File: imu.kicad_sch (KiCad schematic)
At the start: 21 parts, among them J1 Conn_01x06, U1 LSM6DSL, U2 LIS2MDL, U3 AMS1117-3.3

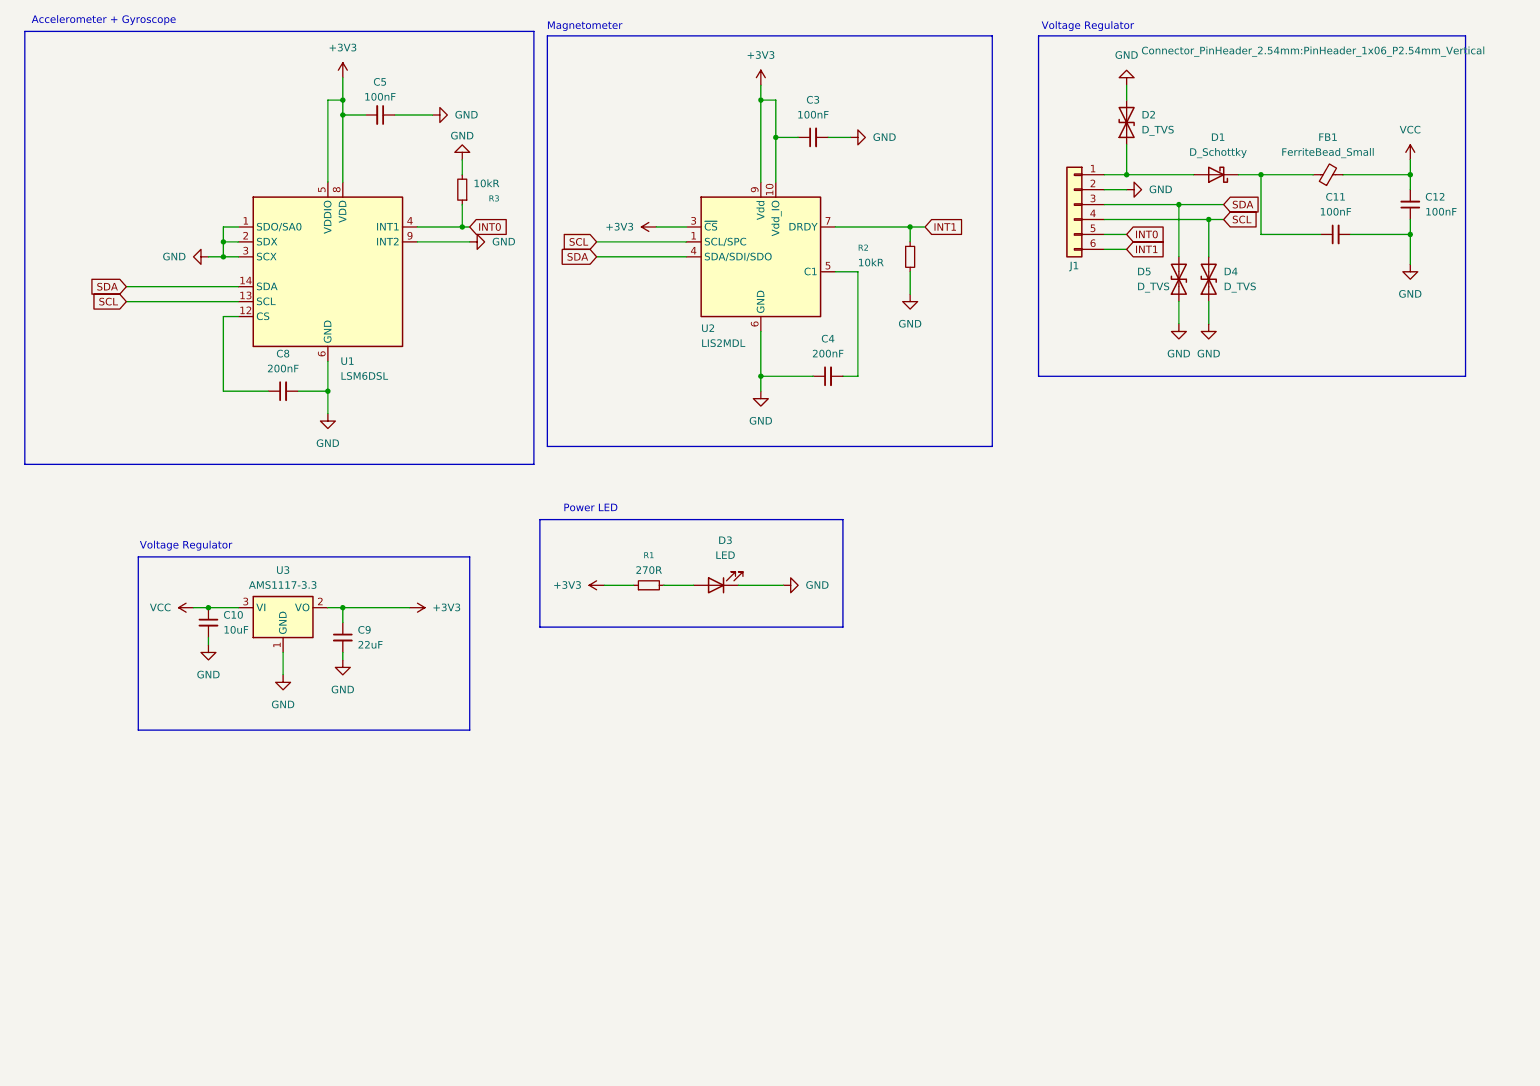
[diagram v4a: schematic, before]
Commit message: Add Fabrication Outputs
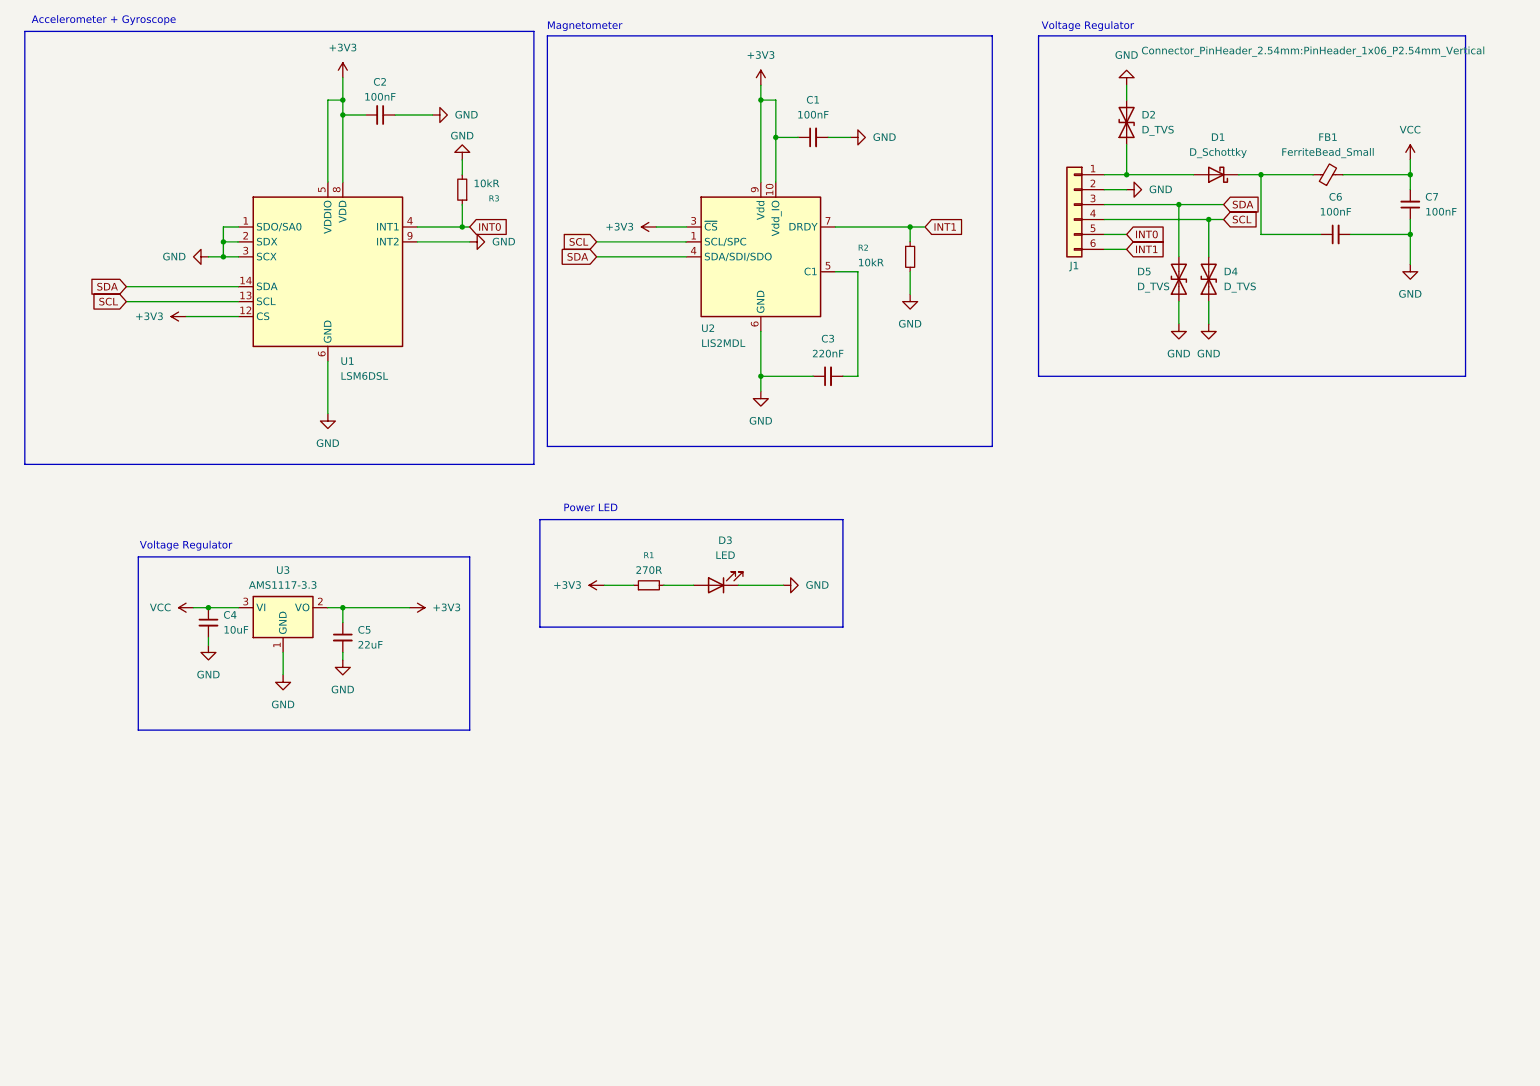
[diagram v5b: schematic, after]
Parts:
- removed C8: 200nF, Capacitor_SMD:C_0805_2012Metric_Pad1.18x1.45mm_HandSolder, symbol Device:C_Small
- C3: renamed from C4; value 200nF -> 220nF
- renumbered C3 to C1, C5 to C2, C10 to C4, C9 to C5, C11 to C6, C12 to C7
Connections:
- net +3V3: now also U1.12 (CS)
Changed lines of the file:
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@@
 	)
 	(junction
-		(at 73.66 78.74)
-		(diameter 0)
-		(color 0 0 0 0)
-	)
-	(junction
 		(at 53.34 115.57)
 		(diameter 0)
@@
 	(wire
 		(pts
-			(xy 55.88 78.74) (xy 63.5 78.74)
+			(xy 49.53 66.04) (xy 58.42 66.04)
 		)
 		(stroke
@@
 	(wire
 		(pts
-			(xy 55.88 66.04) (xy 55.88 78.74)
-		)
-		(stroke
-			(width 0)
-			(type default)
-		)
-	)
-	(wire
-		(pts
 			(xy 209.55 41.91) (xy 220.98 41.91)
 		)
@@
 	(wire
 		(pts
-			(xy 73.66 73.66) (xy 73.66 78.74)
+			(xy 73.66 73.66) (xy 73.66 82.55)
 		)
 		(stroke
@@
 	(wire
 		(pts
-			(xy 58.42 66.04) (xy 55.88 66.04)
-		)
-		(stroke
-			(width 0)
-			(type default)
-		)
-	)
-	(wire
-		(pts
 			(xy 247.65 52.07) (xy 257.81 52.07)
 		)
@@
 	(wire
 		(pts
-			(xy 68.58 78.74) (xy 73.66 78.74)
-		)
-		(stroke
-			(width 0)
-			(type default)
-		)
-	)
-	(wire
-		(pts
 			(xy 205.74 44.45) (xy 209.55 44.45)
 		)
@@
 	(wire
 		(pts
-			(xy 73.66 78.74) (xy 73.66 82.55)
-		)
-		(stroke
-			(width 0)
-			(type default)
-		)
-	)
-	(wire
-		(pts
 			(xy 119.38 53.34) (xy 134.62 53.34)
 		)
@@
 	(symbol
 		(lib_id "power:+3V3")
+		(at 49.53 66.04 90)
+		(unit 1)
+		(exclude_from_sim no)
+		(in_bom yes)
+		(on_board yes)
+		(dnp no)
+		(fields_autoplaced yes)
+		(property "Reference" "#PWR04"
+			(at 53.34 66.04 0)
+			(effects
+				(font
+					(size 1.27 1.27)
+				)
+				(hide yes)
+			)
+		)
+		(property "Value" "+3V3"
+			(at 45.72 66.0399 90)
+			(effects
+				(font
+					(size 1.27 1.27)
+				)
+				(justify left)
+			)
+		)
+		(property "Footprint" ""
+			(at 49.53 66.04 0)
+			(effects
+				(font
+					(size 1.27 1.27)
+				)
+				(hide yes)
+			)
+		)
+		(property "Datasheet" ""
+			(at 49.53 66.04 0)
+			(effects
+				(font
+					(size 1.27 1.27)
+				)
+				(hide yes)
+			)
+		)
+		(property "Description" "Power symbol creates a global label with name \"+3V3\""
+			(at 49.53 66.04 0)
+			(effects
+				(font
+					(size 1.27 1.27)
+				)
+				(hide yes)
+			)
+		)
+		(pin "1"
+		)
+		(instances
+			(project "imu"
+				(path "/c0c3b276-ae23-48c2-9824-bf30dce5574d"
+					(reference "#PWR04")
+					(unit 1)
+				)
+			)
+		)
+	)
+	(symbol
+		(lib_id "power:+3V3")
 		(at 147.32 26.67 0)
 		(unit 1)
@@
 		(dnp no)
 		(fields_autoplaced yes)
-		(property "Reference" "C3"
+		(property "Reference" "C1"
 			(at 156.2163 29.21 90)
 			(effects
@@
 			(project ""
 				(path "/c0c3b276-ae23-48c2-9824-bf30dce5574d"
-					(reference "C3")
+					(reference "C1")
 					(unit 1)
 				)
@@
 		(dnp no)
 		(fields_autoplaced yes)
-		(property "Reference" "C10"
+		(property "Reference" "C4"
 			(at 55.88 116.8462 0)
 			(effects
@@
 			(project ""
 				(path "/c0c3b276-ae23-48c2-9824-bf30dce5574d"
-					(reference "C10")
+					(reference "C4")
 					(unit 1)
 				)
@@
 		(dnp no)
 		(fields_autoplaced yes)
-		(property "Reference" "C12"
+		(property "Reference" "C7"
 			(at 260.35 45.7135 0)
 			(effects
@@
 			(project "imu"
 				(path "/c0c3b276-ae23-48c2-9824-bf30dce5574d"
-					(reference "C12")
+					(reference "C7")
 					(unit 1)
 				)
@@
 		(dnp no)
 		(fields_autoplaced yes)
-		(property "Reference" "C4"
+		(property "Reference" "C3"
 			(at 158.7563 69.85 90)
 			(effects
@@
 			)
 		)
-		(property "Value" "200nF"
+		(property "Value" "220nF"
 			(at 158.7563 72.39 90)
 			(effects
@@
 			(project ""
 				(path "/c0c3b276-ae23-48c2-9824-bf30dce5574d"
-					(reference "C4")
+					(reference "C3")
 					(unit 1)
 				)
@@
 	)
 	(symbol
-		(lib_id "Device:C_Small")
-		(at 66.04 78.74 90)
-		(unit 1)
-		(exclude_from_sim no)
-		(in_bom yes)
-		(on_board yes)
-		(dnp no)
-		(fields_autoplaced yes)
-		(property "Reference" "C8"
-			(at 66.0463 72.39 90)
-			(effects
-				(font
-					(size 1.27 1.27)
-				)
-			)
-		)
-		(property "Value" "200nF"
-			(at 66.0463 74.93 90)
-			(effects
-				(font
-					(size 1.27 1.27)
-				)
-			)
-		)
-		(property "Footprint" "Capacitor_SMD:C_0805_2012Metric_Pad1.18x1.45mm_HandSolder"
-			(at 66.04 78.74 0)
-			(effects
-				(font
-					(size 1.27 1.27)
-				)
-				(hide yes)
-			)
-		)
-		(property "Datasheet" "~"
-			(at 66.04 78.74 0)
-			(effects
-				(font
-					(size 1.27 1.27)
-				)
-				(hide yes)
-			)
-		)
-		(property "Description" "Unpolarized capacitor, small symbol"
-			(at 66.04 78.74 0)
-			(effects
-				(font
-					(size 1.27 1.27)
-				)
-				(hide yes)
-			)
-		)
-		(pin "1"
-		)
-		(pin "2"
-		)
-		(instances
-			(project "imu"
-				(path "/c0c3b276-ae23-48c2-9824-bf30dce5574d"
-					(reference "C8")
-					(unit 1)
-				)
-			)
-		)
-	)
-	(symbol
 		(lib_id "Device:D_TVS")
 		(at 218.44 59.69 90)
@@
 		(on_board yes)
 		(dnp no)
-		(property "Reference" "C5"
+		(property "Reference" "C2"
 			(at 82.55 26.162 90)
 			(effects
@@
 			(project "imu"
 				(path "/c0c3b276-ae23-48c2-9824-bf30dce5574d"
-					(reference "C5")
+					(reference "C2")
 					(unit 1)
 				)
@@
 		(dnp no)
 		(fields_autoplaced yes)
-		(property "Reference" "C9"
+		(property "Reference" "C5"
 			(at 78.74 119.3862 0)
 			(effects
@@
 			(project ""
 				(path "/c0c3b276-ae23-48c2-9824-bf30dce5574d"
-					(reference "C9")
+					(reference "C5")
 					(unit 1)
 				)
@@
 		(dnp no)
 		(fields_autoplaced yes)
-		(property "Reference" "C11"
+		(property "Reference" "C6"
 			(at 245.1163 45.72 90)
 			(effects
@@
 			(project "imu"
 				(path "/c0c3b276-ae23-48c2-9824-bf30dce5574d"
-					(reference "C11")
+					(reference "C6")
 					(unit 1)
 				)

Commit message: Add ESP32 and USB-C Recep to Schematic
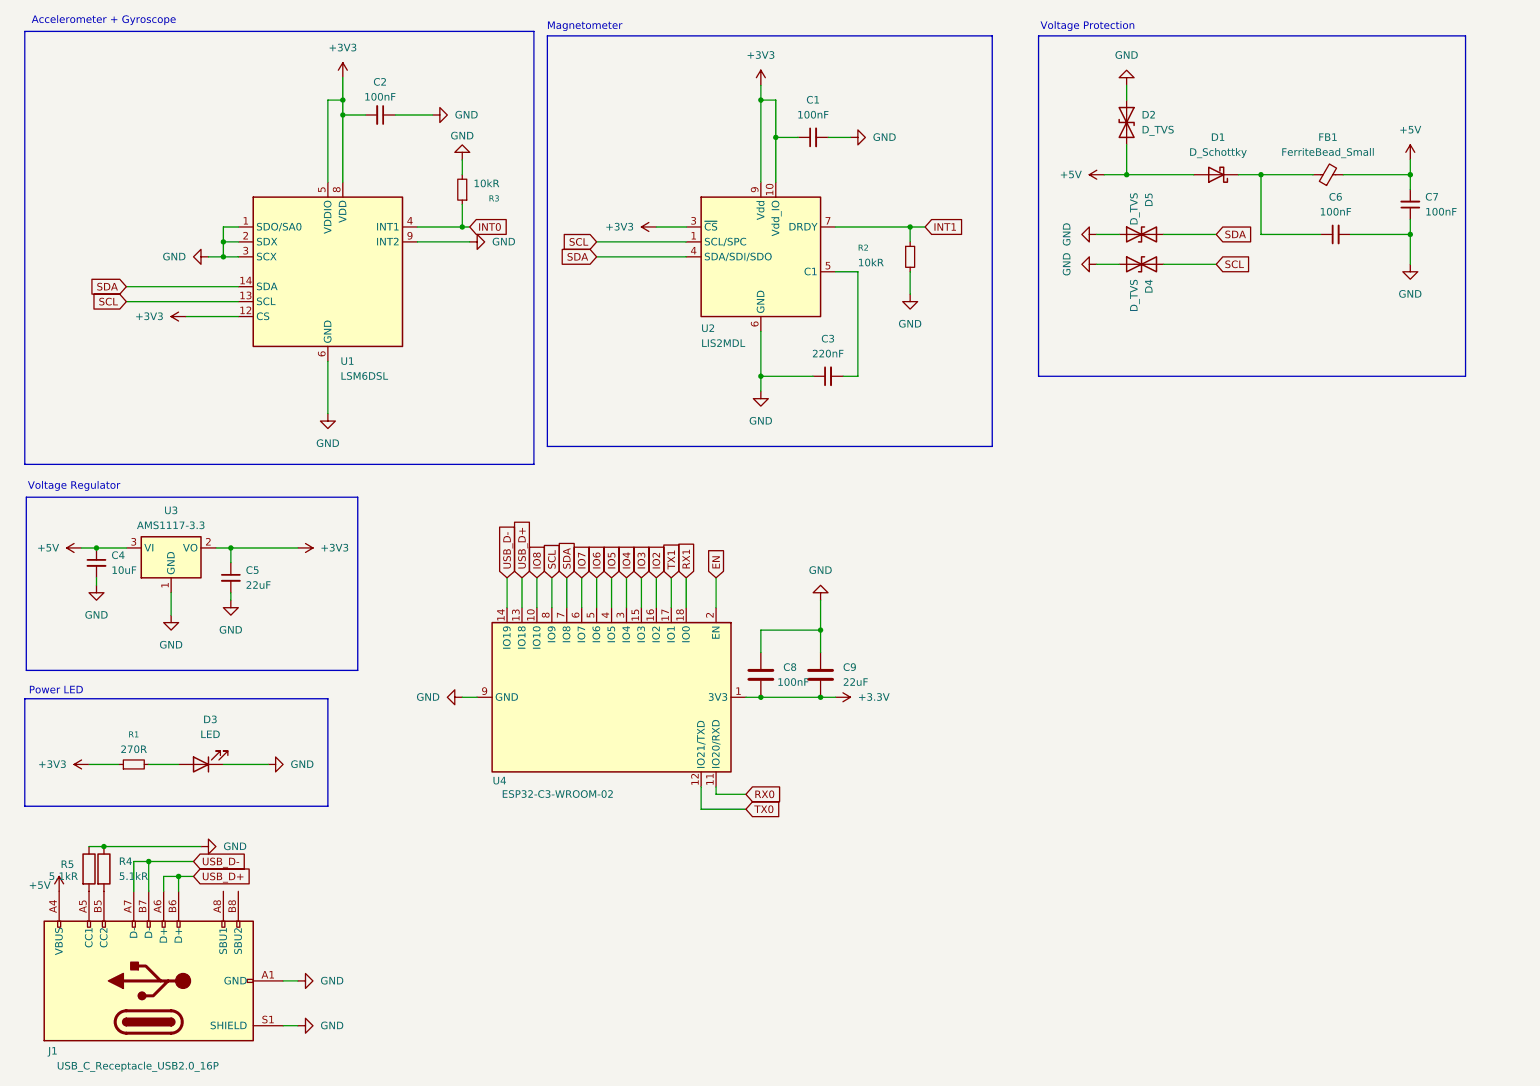
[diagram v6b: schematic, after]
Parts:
- removed J1: Conn_01x06, Connector_PinHeader_2.54mm:PinHeader_1x06_P2.54mm_Vertical, symbol Connector_Generic:Conn_01x06
- added C8: 100nF, symbol Device:C
- added C9: 22uF, symbol Device:C
- added J1: USB_C_Receptacle_USB2.0_16P, symbol Connector:USB_C_Receptacle_USB2.0_16P
- added R4, R5: 5.1kR, symbol Device:R
- added U4: ESP32-C3-WROOM-02, RF_Module:ESP32-C3-WROOM-02, symbol RF_Module:ESP32-C3-WROOM-02
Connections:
- net VCC is gone; now on net +5V: C4.1, C7.2, FB1.2, U3.3 (VI)
- net GND: now also D2.1 (A1), C8.1, C9.1, J1.A1 (GND), J1.A12 (GND), J1.B1 (GND), J1.B12 (GND), J1.S1 (SHIELD), R4.1, R5.1, U4.19 (GND), U4.9 (GND); no longer D2.2 (A2)
- net SCL: now also U4.8 (IO9)
- net SDA: now also U4.7 (IO8)
- net +5V: now reaches D1.2 (A)
- net +5V: now also D2.2 (A2), J1.A4 (VBUS), J1.A9 (VBUS), J1.B4 (VBUS), J1.B9 (VBUS); no longer D2.1 (A1)
- new net: J1.A5 (CC1), R5.2
- new net: J1.B5 (CC2), R4.2
- new net +3.3V: C8.2, C9.2, U4.1 (3V3)
- new net EN: U4.2 (EN)
- new net IO2: U4.16 (IO2)
- new net IO3: U4.15 (IO3)
- new net IO4: U4.3 (IO4)
- new net IO5: U4.4 (IO5)
- new net IO6: U4.5 (IO6)
- new net IO7: U4.6 (IO7)
- new net IO8: U4.10 (IO10)
- new net RX0: U4.11 (IO20/RXD)
- new net RX1: U4.18 (IO0)
- new net TX0: U4.12 (IO21/TXD)
- new net TX1: U4.17 (IO1)
- new net USB_D+: J1.A6 (D+), J1.B6 (D+), U4.13 (IO18)
- new net USB_D-: J1.A7 (D-), J1.B7 (D-), U4.14 (IO19)
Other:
- note added: "Voltage Protection"
- moved on the sheet: C4, C5, D2, D3, D4, D5, R1, U3

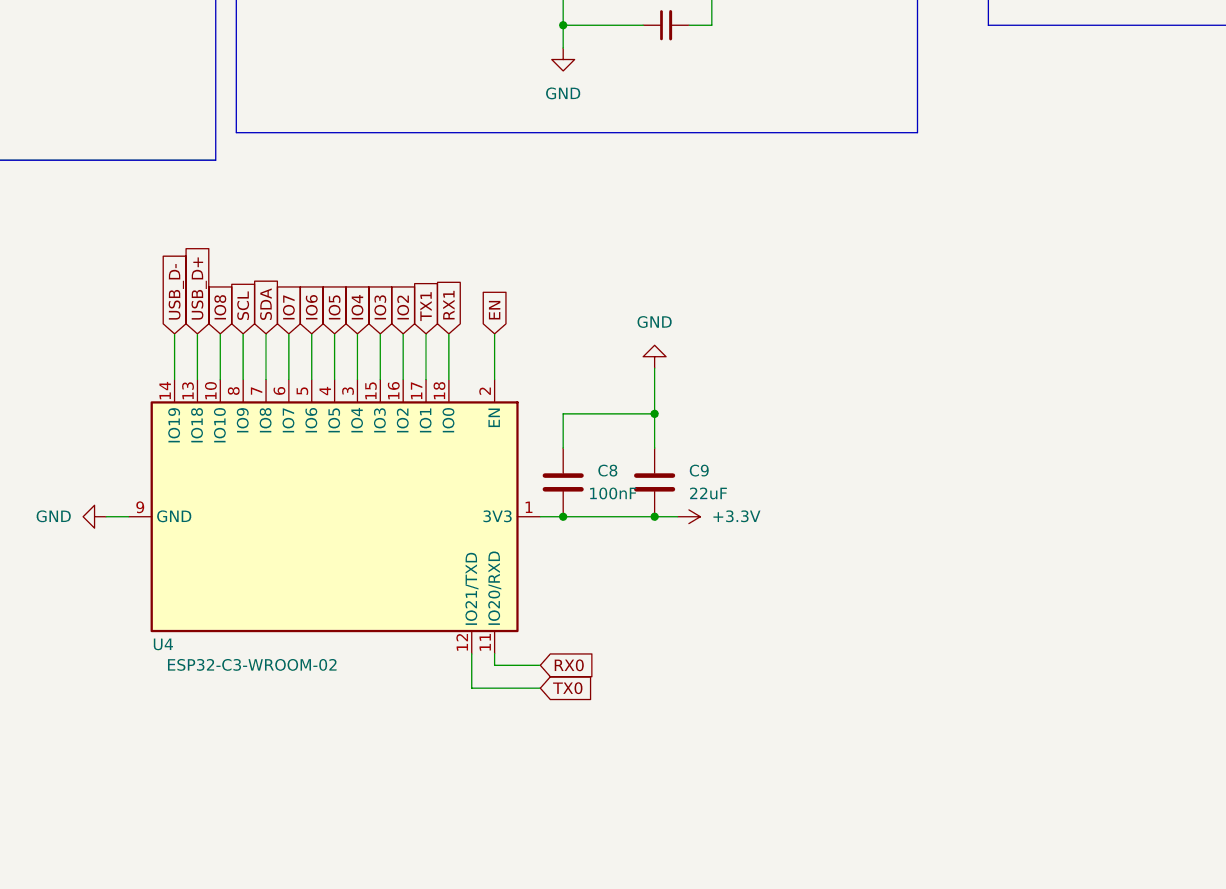
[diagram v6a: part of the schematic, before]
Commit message: Add EN and BOOT Push Buttons
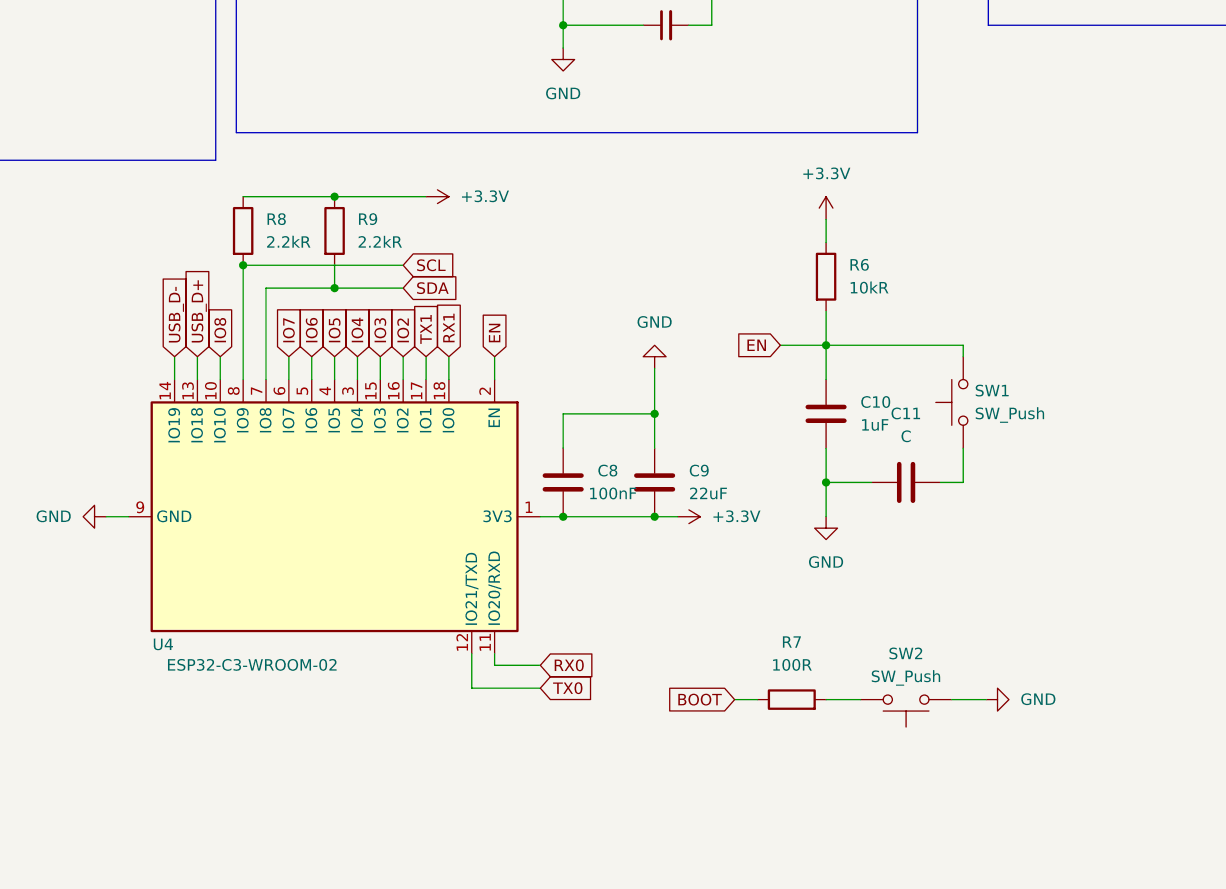
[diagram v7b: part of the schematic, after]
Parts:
- added C10: 1uF, symbol Device:C
- added C11: C, symbol Device:C
- added R6: 10kR, symbol Device:R
- added R7: 100R, symbol Device:R
- added R8, R9: 2.2kR, symbol Device:R
- added SW1, SW2: SW_Push, symbol Switch:SW_Push
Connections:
- net +3.3V: now also R6.1, R8.1, R9.1
- net EN: now also C10.1, R6.2, SW1.2
- net GND: now also C10.2, C11.1, SW2.1
- net SCL: now also R8.2
- net SDA: now also R9.2
- new net: C11.2, SW1.1
- new net: R7.2, SW2.2
- new net BOOT: R7.1
